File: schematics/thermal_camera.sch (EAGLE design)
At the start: 42 parts, among them IC1 PIC16F876SO, Q3 FS8205A, SW1 CT10-XXXX-A2, X1 MINI-USB-32005-201

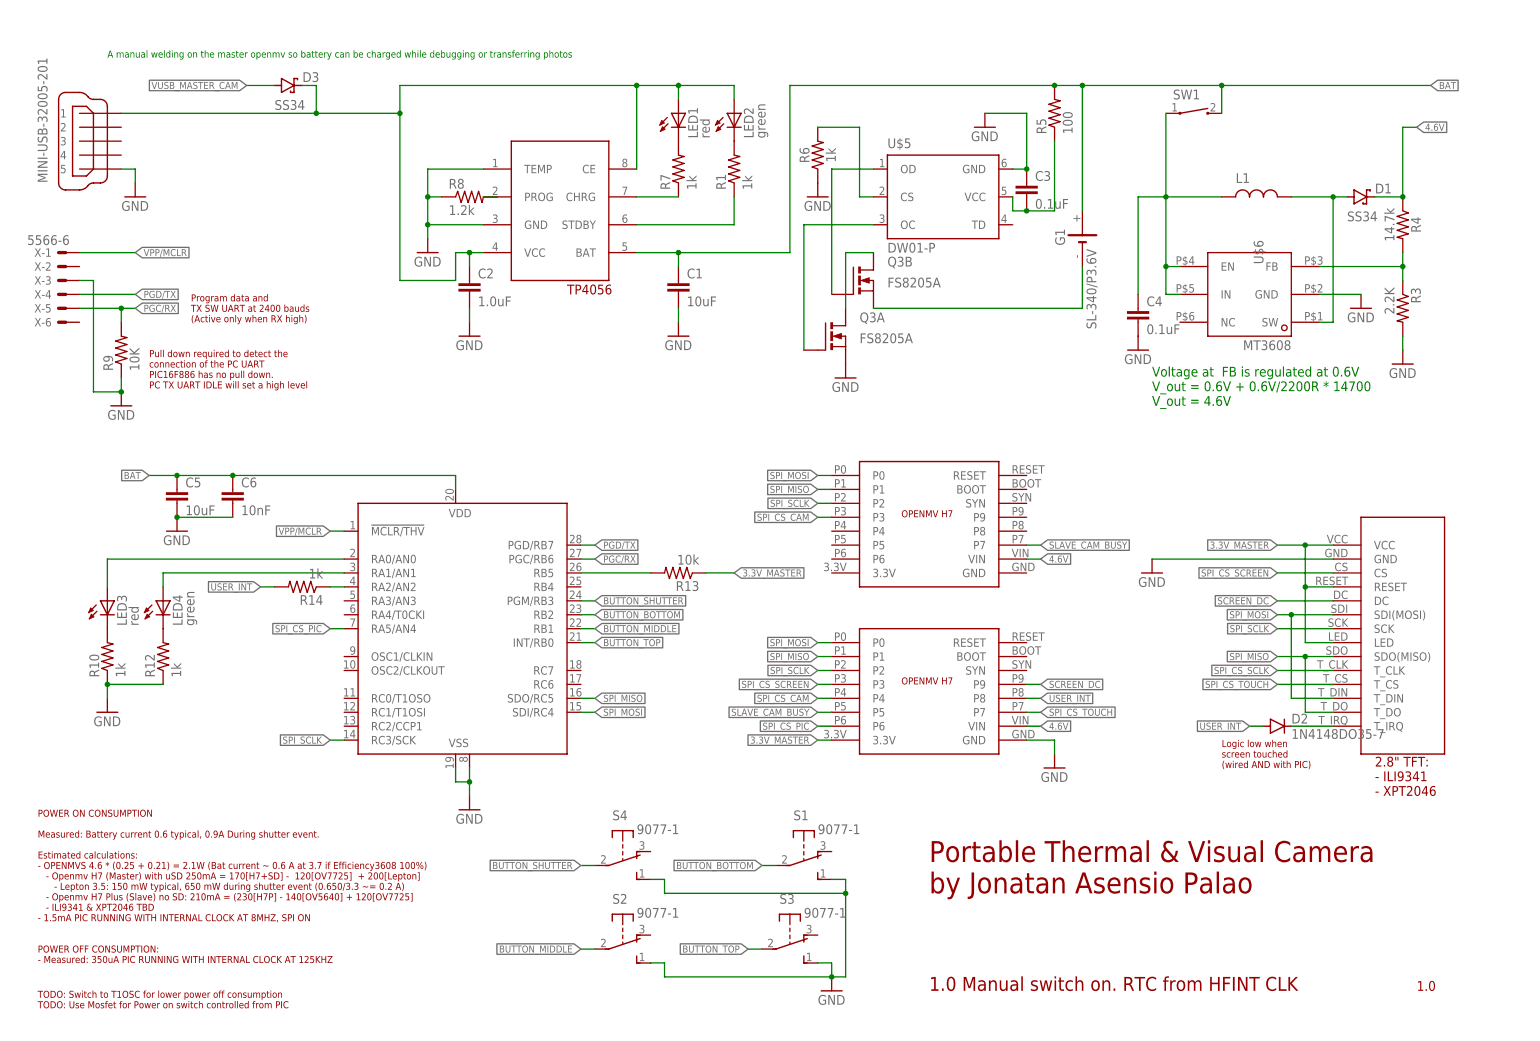
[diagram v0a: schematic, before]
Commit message: PIC RTC switched to a 32kHz crystal Other further power optimizations
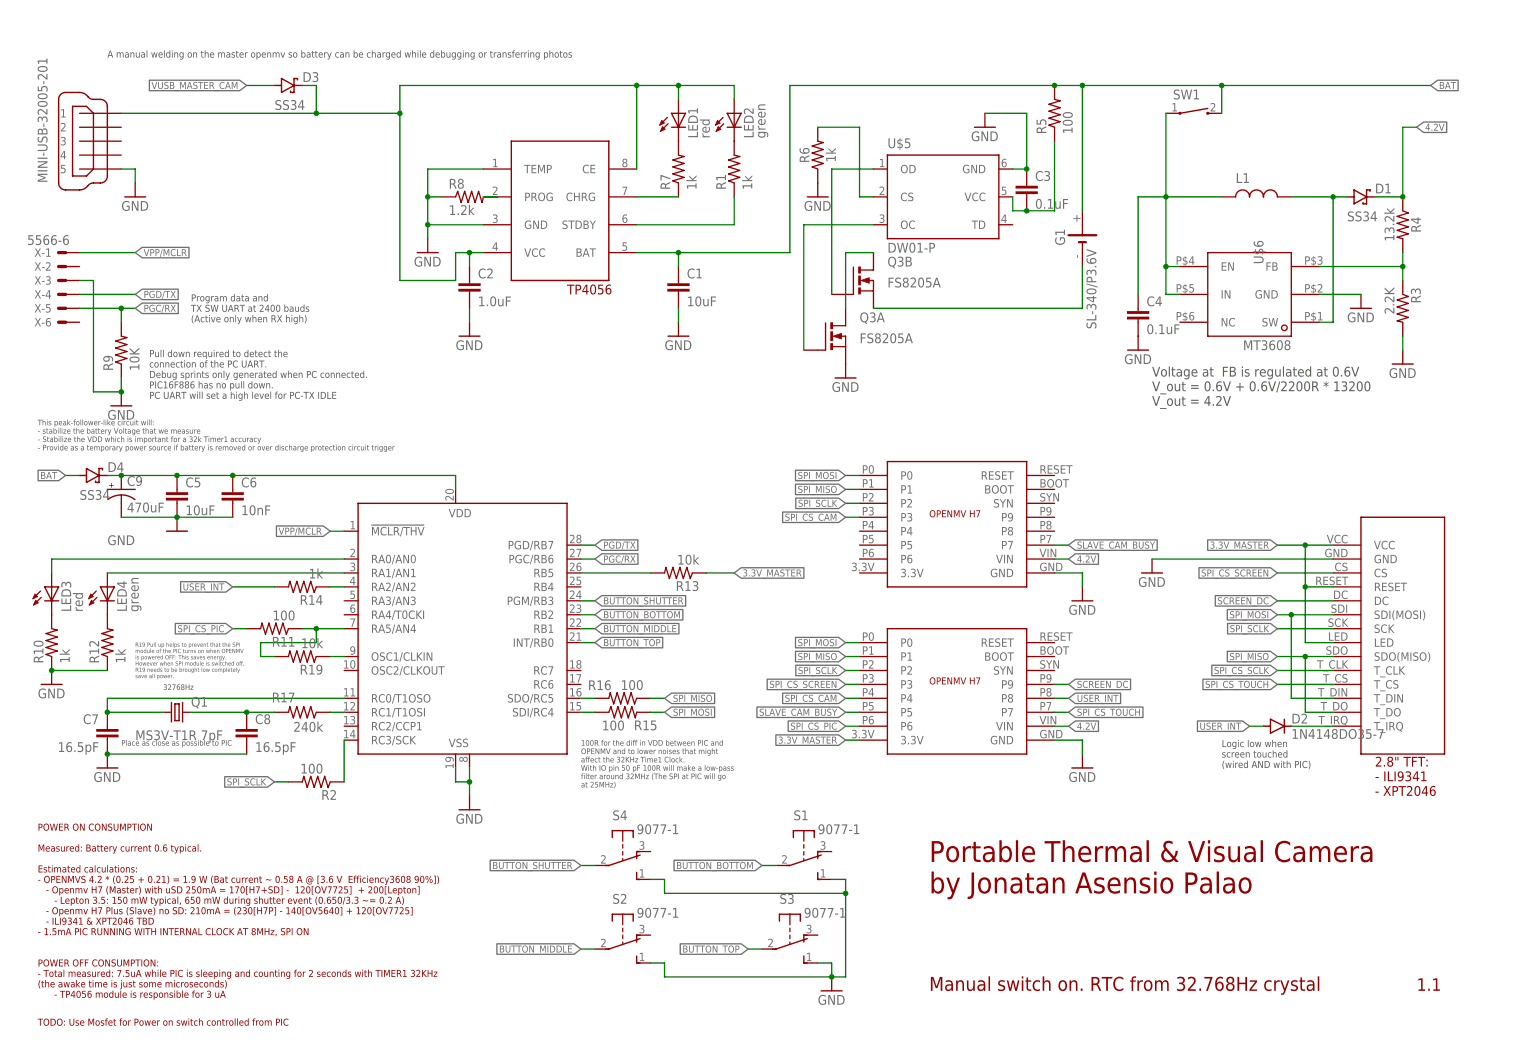
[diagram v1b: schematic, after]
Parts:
- added C7, C8: 16.5pF, SparkFun-Capacitors:10UF-1206-6.3V-20%
- added C9: 470uF, rcl:CPOL-US153CLV-0505
- added D4: SS34, zetex:DS_E2L
- added Q1: MS3V-T1R 7pF, crystal:FC-12M
- added R11, R15, R16, R2: 100, rcl:R-US_0204/7
- added R17: 240k, rcl:R-US_0204/7
- added R19: 10k, rcl:R-US_0204/7
- R4: value 14.7k -> 13.2k
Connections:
- net 4.6V renamed 4.2V
- new net N$14: IC1.RC3/SCK, R2.1
- new net N$18: IC1.RA5/AN4, R11.1, R19.2
- new net N$21: IC1.OSC1/CLKIN, R19.1
- new net N$24: IC1.RC1/T1OSI, R17.1
- new net N$25: C7.1, IC1.RC0/T1OSO, Q1.1
- new net N$26: C8.1, Q1.2, R17.2
- net BAT: now also C9.+, D4.A, D4.K
- net GND: now also C7.2, C8.2, C9.-, U$2.GND
- net SPI_CS_PIC: now also R11.2; no longer IC1.RA5/AN4
- net SPI_MISO: now also R15.1, R15.2
- net SPI_MOSI: now also R16.1, R16.2
- net SPI_SCLK: now also R2.2; no longer IC1.RC3/SCK
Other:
- note added: "1.1"
- note added: "100R for the diff in VDD between PIC and OPENMV and to lower noises that might affect the 32KHz Time1 Clock. With IO pin 50 pF 100R will make a low-pass filter around 32MHz (The SPI at PIC will go at 25MHz)"
- note added: "32768Hz"
- note added: "MT3608 battery voltage module"
- note added: "Manual switch on. RTC from 32.768Hz crystal"
- note added: "POWER ON CONSUMPTION Measured: Battery current 0.6 typical. Estimated calculations: - OPENMVS 4.2 * (0.25 + 0.21) = 1.9 W (Bat current ~ 0.58 A @ [3.6 V Efficiency3608 90%]) - Openmv H7 (Master) with uSD 250mA = 170[H7+SD] - 120[OV7725] + 200[Lepton] - Lepton 3.5: 150 mW typical, 650 mW during shutter event (0.650/3.3 ~= 0.2 A) - Openmv H7 Plus (Slave) no SD: 210mA = (230[H7P] - 140[OV5640] + 120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"
- note added: "Place as close as possible to PIC"
- note added: "Pull down required to detect the connection of the PC UART. Debug sprints only generated when PC connected. PIC16F886 has no pull down. PC UART will set a high level for PC-TX IDLE"
- note added: "R19 Pull up helps to prevent that the SPI module of the PIC turns on when OPENMV is powered OFF: This saves energy. However when SPI module is switched off, R19 needs to be brought low completely save all power."
- note added: "TODO: Use Mosfet for Power on switch controlled from PIC"
- note added: "This peak-follower-like circuit will: - stabilize the battery Voltage that we measure - Stabilize the VDD which is important for a 32k Timer1 accuracy - Provide as a temporary power source if battery is removed or over discharge protection circuit trigger"
- note added: "Voltage at FB is regulated at 0.6V V_out = 0.6V + 0.6V/2200R * 13200 V_out = 4.2V"
- note removed: "1.0"
- note removed: "1.0 Manual switch on. RTC from HFINT CLK"
- note removed: "BOOST battery voltage module"
- note removed: "POWER ON CONSUMPTION Measured: Battery current 0.6 typical, 0.9A During shutter event. Estimated calculations: - OPENMVS 4.6 * (0.25 + 0.21) = 2.1W (Bat current ~ 0.6 A at 3.7 if Efficiency3608 100%) - Openmv H7 (Master) with uSD 250mA = 170[H7+SD] - 120[OV7725] + 200[Lepton] - Lepton 3.5: 150 mW typical, 650 mW during shutter event (0.650/3.3 ~= 0.2 A) - Openmv H7 Plus (Slave) no SD: 210mA = (23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"
- note removed: "Pull down required to detect the connection of the PC UART PIC16F886 has no pull down. PC TX UART IDLE will set a high level"
- note removed: "TODO: Switch to T1OSC for lower power off consumption TODO: Use Mosfet for Power on switch controlled from PIC"
- note removed: "Voltage at FB is regulated at 0.6V V_out = 0.6V + 0.6V/2200R * 14700 V_out = 4.6V"
- moved on the sheet: LED3, LED4, R10, R12
